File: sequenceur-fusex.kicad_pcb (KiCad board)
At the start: 2 copper layers, 67 x 48 mm, 29 parts, among them J1 ALIM 12v, J2 ELECTRO AIMANT PERMANANT, J3 JACK M/A NF, J4 JACK DEP NF, Q1 IRLZ44N, Q2 IRLZ44N, U1 LM324

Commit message: inlarge power tracks + add text
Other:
- net class power added: clearance 0.254, trace_width 0.45, via_dia 0.6, via_drill 0.4
- board text added: "Parachute Sequencer http://github.com/fusex/"

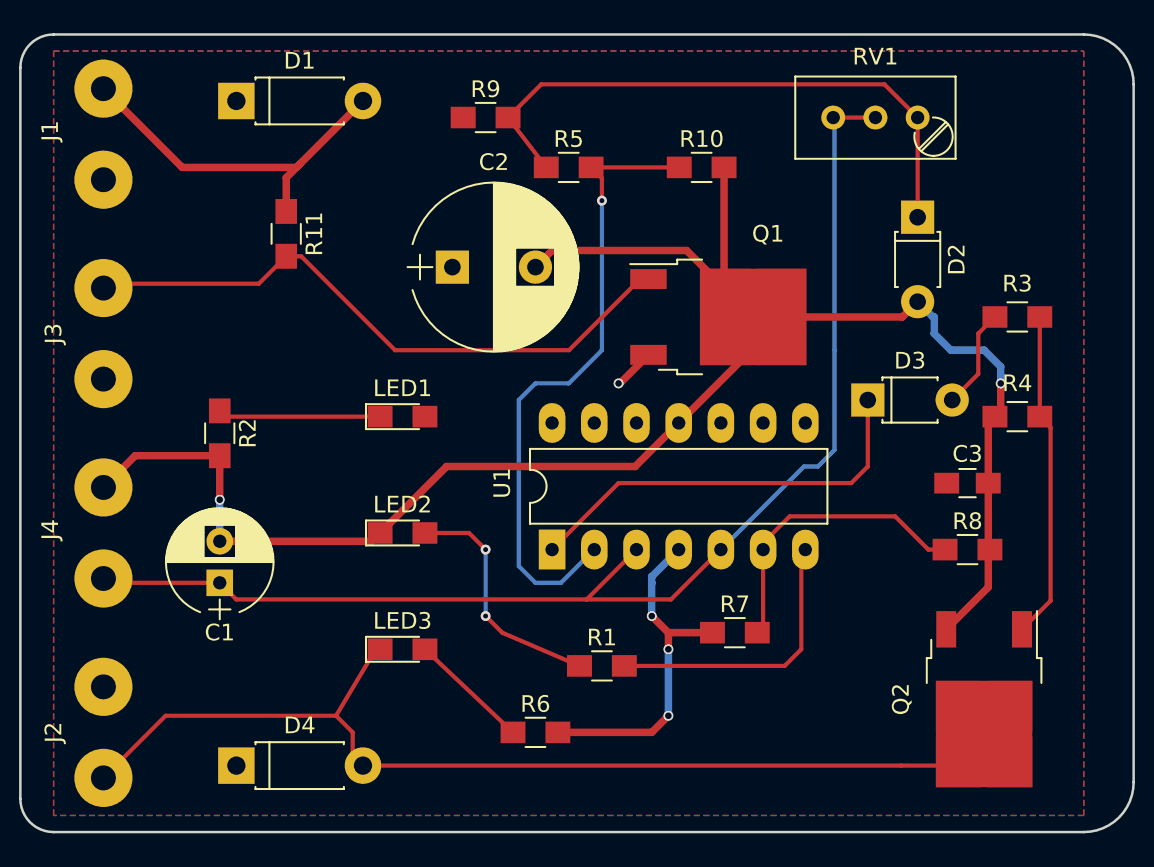
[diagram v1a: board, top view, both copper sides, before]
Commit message: add a fuse and enlarge some track
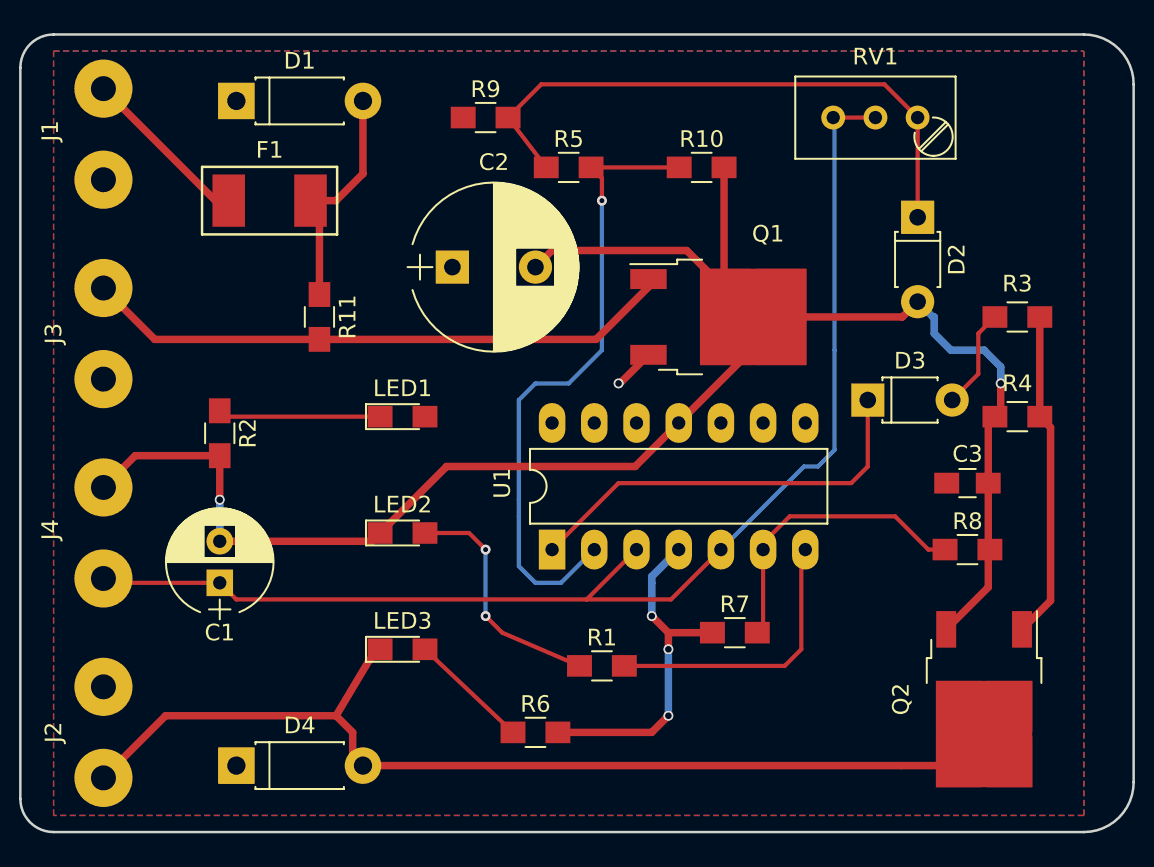
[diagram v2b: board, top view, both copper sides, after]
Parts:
- added F1: Fuse, fuse:NANO2_SMD, F.Cu at (114.0, 65.0)
- added REF***: KiCad-Logo2_6mm_SilkScreen, Symbols:KiCad-Logo2_6mm_SilkScreen, B.Cu at (151.0, 94.0)
- moved R11 5.39 mm to (117.0, 72.0)
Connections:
- J1 pad 2: Net-(D1-Pad2) -> Net-(F1-Pad2)
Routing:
- net Net-(F1-Pad2): track 0.00 -> 10.3 mm
- net Net-(D1-Pad2): track 22.4 -> 14.1 mm
- net Net-(J3-Pad1): track 37.7 -> 36.7 mm

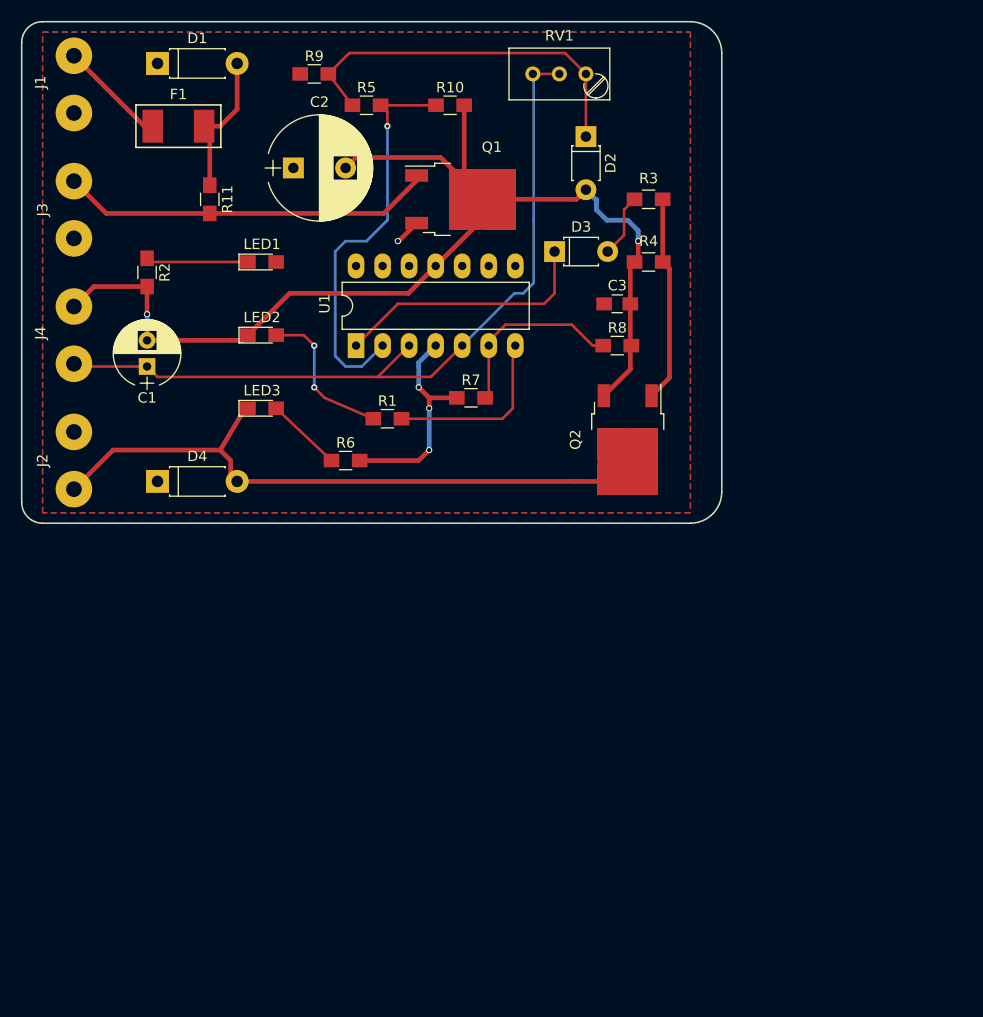
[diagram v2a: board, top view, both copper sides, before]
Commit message: select smt instead of though-holes
update symbol and cache file for kicadv5

delete net list
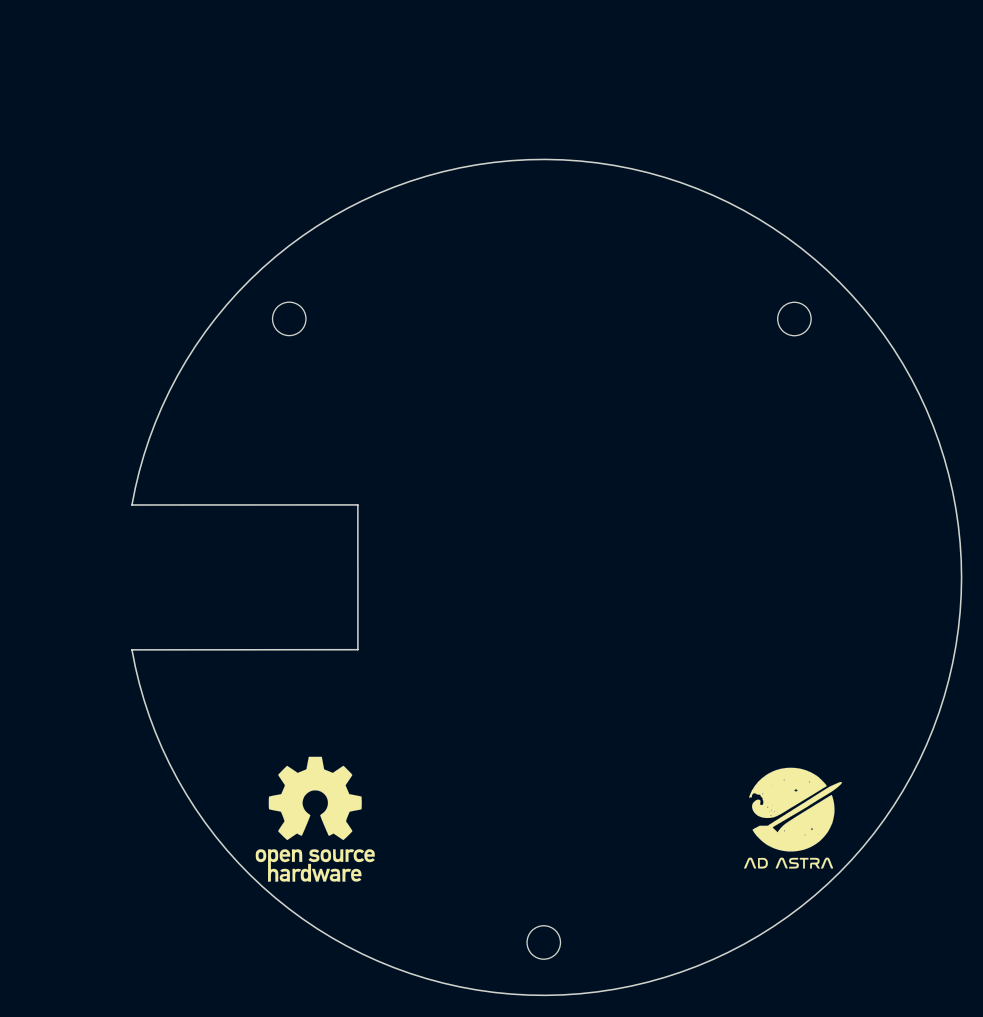
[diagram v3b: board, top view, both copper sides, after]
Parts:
- removed C1: 47uF, Capacitors_THT:CP_Radial_D6.3mm_P2.50mm
- removed C2: 470uF, Capacitors_THT:CP_Radial_D10.0mm_P5.00mm
- removed C3: 100nF, Capacitors_SMD:C_0805_HandSoldering
- removed D1, D4: 1N4007, Diodes_THT:D_DO-41_SOD81_P7.62mm_Horizontal
- removed D2: BZX79C4V7, Diodes_THT:D_T-1_P5.08mm_Horizontal
- removed D3: BZX79C2V4, Diodes_THT:D_T-1_P5.08mm_Horizontal
- removed F1: Fuse, fuse:NANO2_SMD
- removed J1: ALIM 12v, wire:2x_20AWG
- removed J2: ELECTRO AIMANT PERMANANT, wire:2x_20AWG
- removed J3: JACK M/A NF, wire:2x_20AWG
- removed J4: JACK DEP NF, wire:2x_20AWG
- removed LED1: SEQ ACTIF, LEDs:LED_0805_HandSoldering
- removed LED2: DECO, LEDs:LED_0805_HandSoldering
- removed LED3: ACT ACTIF, LEDs:LED_0805_HandSoldering
- removed Q1, Q2: IRLZ44N, TO_SOT_Packages_SMD:TO-252-2
- removed R1, R2, R3, R6, R8, R9: 1k, Resistors_SMD:R_0805_HandSoldering
- removed R10, R5: 10k, Resistors_SMD:R_0805_HandSoldering
- removed R11, R4: 100k, Resistors_SMD:R_0805_HandSoldering
- removed R7: 1M, Resistors_SMD:R_0805_HandSoldering
- removed REF***: KiCad-Logo2_6mm_SilkScreen, Symbols:KiCad-Logo2_6mm_SilkScreen
- removed RV1: 1M, Potentiometers:Potentiometer_Trimmer_Bourns_3296W
- removed U1: LM324, Housings_DIP:DIP-14_W7.62mm_LongPads
- added G***: LOGO, artworks:adastra6, F.Cu at (172.7, 131.2)
- added M1: MountingHole_3.2mm_M3, MountingHole:MountingHole_3.2mm_M3, F.Cu at (149.0, 143.1)
- added M2: MountingHole_3.2mm_M3, MountingHole:MountingHole_3.2mm_M3, F.Cu at (173.0, 83.5)
- added M3: MountingHole_3.2mm_M3, MountingHole:MountingHole_3.2mm_M3, F.Cu at (124.6, 83.4)
- added REF**: OSHW-Logo_11.4x12mm_SilkScreen, Symbol:OSHW-Logo_11.4x12mm_SilkScreen, F.Cu at (127.1, 131.3)
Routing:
- net Net-(C1-Pad2): track 113.4 -> 0.00 mm, vias 2 -> 0
- net Net-(C1-Pad1): track 75.1 -> 0.00 mm
- net Net-(D4-Pad2): track 62.2 -> 0.00 mm
- net Net-(R10-Pad1): track 38.6 -> 0.00 mm, vias 1 -> 0
- net Net-(J3-Pad1): track 36.7 -> 0.00 mm
- net Net-(D2-Pad1): track 36.1 -> 0.00 mm
- net Net-(D3-Pad1): track 25.1 -> 0.00 mm
- net +12V: track 20.8 -> 0.00 mm, vias 3 -> 0
- net Net-(Q2-Pad1): track 20.2 -> 0.00 mm
- net Net-(R7-Pad2): track 19.0 -> 0.00 mm
- net Net-(R1-Pad2): track 17.5 -> 0.00 mm
- net Net-(LED2-Pad2): track 14.5 -> 0.00 mm, vias 2 -> 0
- net Net-(D1-Pad2): track 14.1 -> 0.00 mm
- net Net-(F1-Pad2): track 10.3 -> 0.00 mm
- net Net-(LED1-Pad1): track 10.3 -> 0.00 mm
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- removed copper zone on F.Cu, net +12V
- removed copper zone on B.Cu, net GND
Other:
- board size 67 x 48 mm -> 79.4 x 80 mm
- board text removed: "Parachute Sequencer http://github.com/fusex/"
